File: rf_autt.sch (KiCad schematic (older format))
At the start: 10 parts, among them U4 FST3253

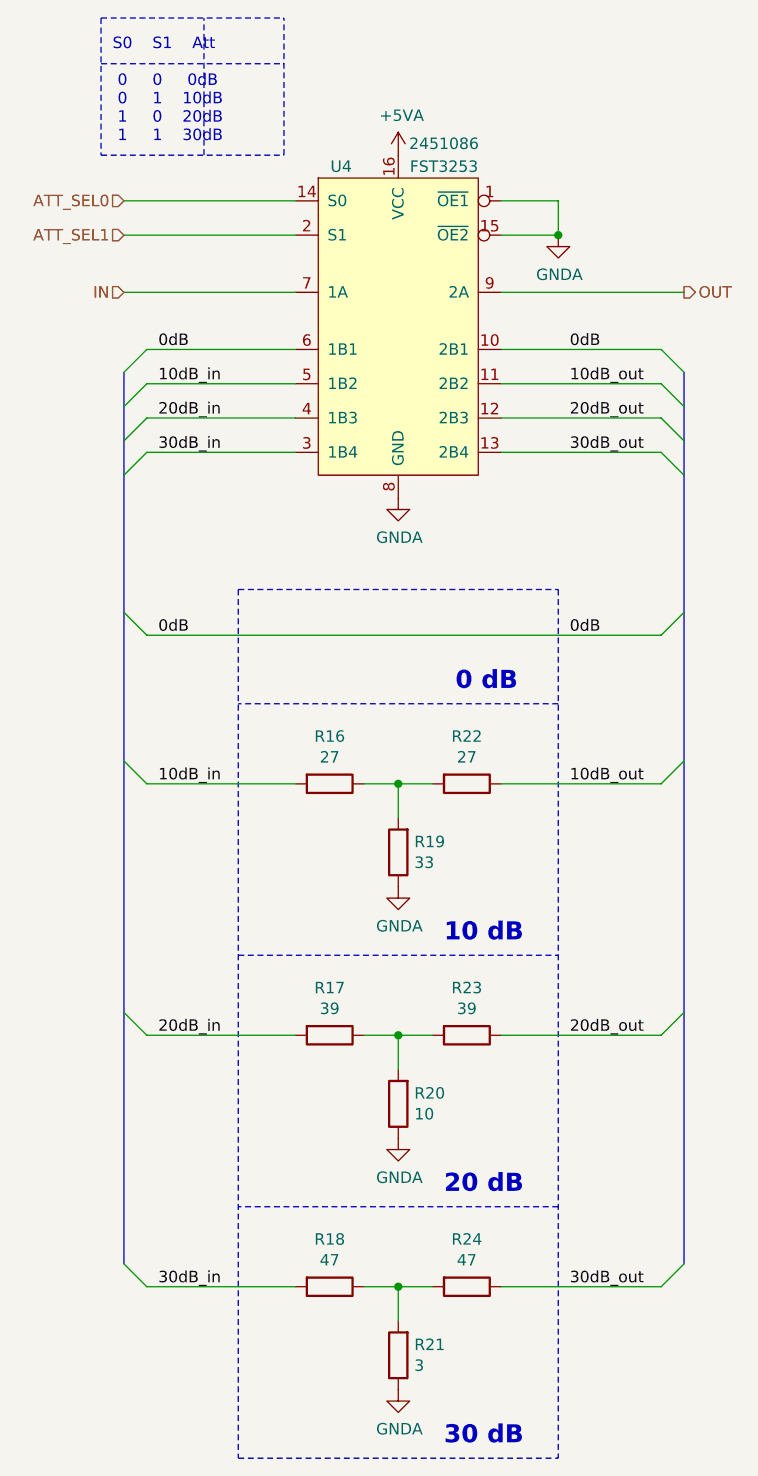
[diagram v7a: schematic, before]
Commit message: FPGA change and new project file
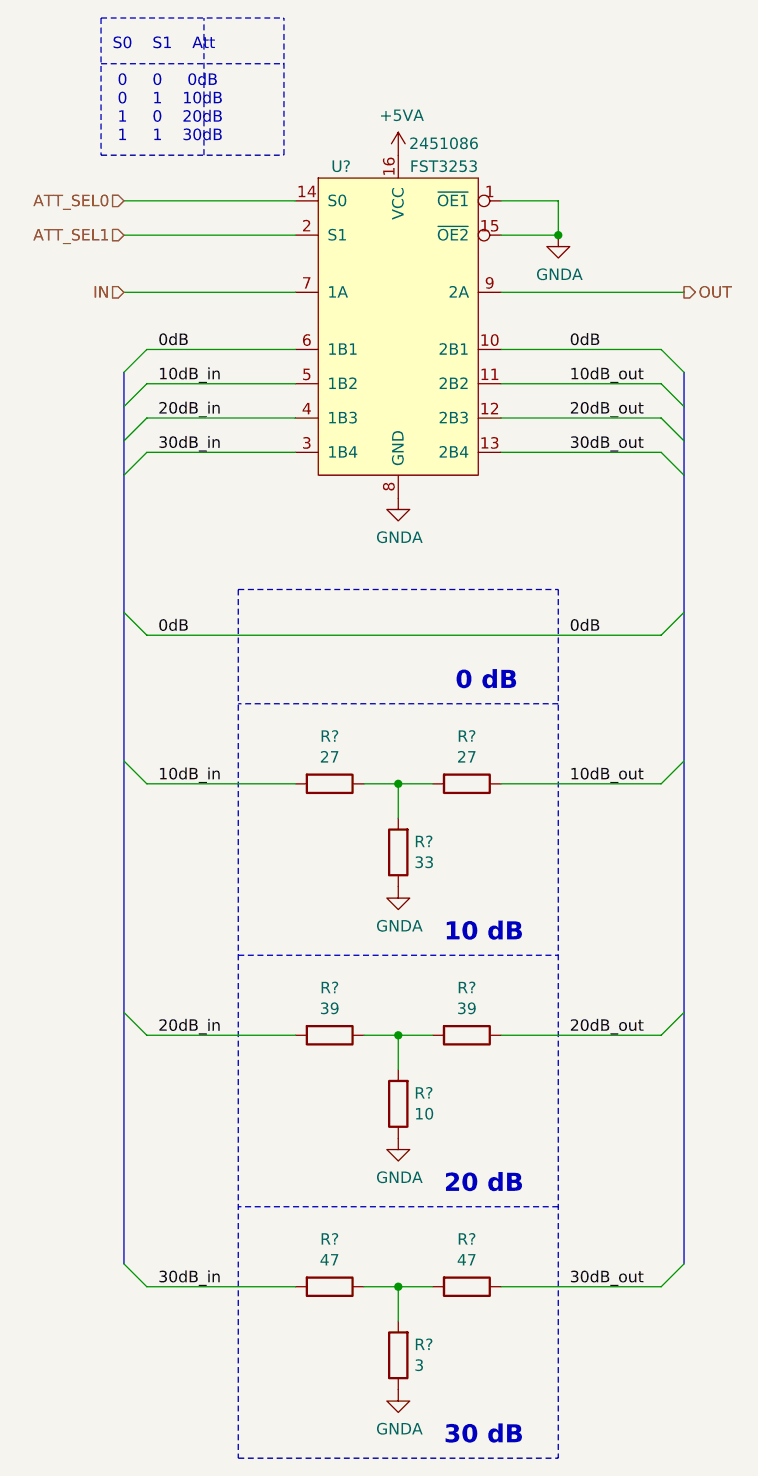
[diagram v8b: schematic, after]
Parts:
- renumbered R19 to R?, R16 to R?, R22 to R?, R21 to R?, R18 to R?, R24 to R?, R20 to R?, R17 to R?, R23 to R?, U4 to U?
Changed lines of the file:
@@
 $Descr A4 11693 8268
 encoding utf-8
-Sheet 7 7
+Sheet 7 12
 Title "HF-SDR RF-Attenuator"
 Date "2020 december"
@@
 OUT
 $Comp
-L sdr:FST3253 U4
+L sdr:FST3253 U?
 U 1 1 5FE50A6B
 P 5600 1900
-F 0 "U4" H 5350 2550 50  0000 C CNN
+F 0 "U?" H 5350 2550 50  0000 C CNN
 F 1 "FST3253" H 5800 2550 50  0000 C CNN
 F 2 "Package_SO:TSSOP-16_4.4x5mm_P0.65mm" H 5600 1900 50  0001 C CNN
@@
 ATT_SEL1
 $Comp
-L power:GNDA #PWR0136
+L power:GNDA #PWR?
 U 1 1 5FE53082
 P 5600 4400
-F 0 "#PWR0136" H 5600 4150 50  0001 C CNN
+F 0 "#PWR?" H 5600 4150 50  0001 C CNN
 F 1 "GNDA" H 5605 4227 50  0000 C CNN
 F 2 "" H 5600 4400 50  0001 C CNN
@@
 $EndComp
 $Comp
-L Device:R R19
+L Device:R R?
 U 1 1 5FE56E4E
 P 5600 4250
-F 0 "R19" H 5530 4204 50  0000 R CNN
+F 0 "R?" H 5530 4204 50  0000 R CNN
 F 1 "33" H 5530 4295 50  0000 R CNN
 F 2 "Resistor_SMD:R_0805_2012Metric_Pad1.20x1.40mm_HandSolder" V 5530 4250 50  0001 C CNN
@@
 $EndComp
 $Comp
-L Device:R R16
+L Device:R R?
 U 1 1 5FE5744A
 P 5300 3950
-F 0 "R16" V 5093 3950 50  0000 C CNN
+F 0 "R?" V 5093 3950 50  0000 C CNN
 F 1 "27" V 5184 3950 50  0000 C CNN
 F 2 "Resistor_SMD:R_0805_2012Metric_Pad1.20x1.40mm_HandSolder" V 5230 3950 50  0001 C CNN
@@
 $EndComp
 $Comp
-L Device:R R22
+L Device:R R?
 U 1 1 5FE57E99
 P 5900 3950
-F 0 "R22" V 5693 3950 50  0000 C CNN
+F 0 "R?" V 5693 3950 50  0000 C CNN
 F 1 "27" V 5784 3950 50  0000 C CNN
 F 2 "Resistor_SMD:R_0805_2012Metric_Pad1.20x1.40mm_HandSolder" V 5830 3950 50  0001 C CNN
@@
 	5600 3950 5750 3950
 $Comp
-L power:GNDA #PWR0137
+L power:GNDA #PWR?
 U 1 1 5FE5C53B
 P 5600 6600
-F 0 "#PWR0137" H 5600 6350 50  0001 C CNN
+F 0 "#PWR?" H 5600 6350 50  0001 C CNN
 F 1 "GNDA" H 5605 6427 50  0000 C CNN
 F 2 "" H 5600 6600 50  0001 C CNN
@@
 $EndComp
 $Comp
-L Device:R R21
+L Device:R R?
 U 1 1 5FE5C541
 P 5600 6450
-F 0 "R21" H 5530 6404 50  0000 R CNN
+F 0 "R?" H 5530 6404 50  0000 R CNN
 F 1 "3" H 5530 6495 50  0000 R CNN
 F 2 "Resistor_SMD:R_0805_2012Metric_Pad1.20x1.40mm_HandSolder" V 5530 6450 50  0001 C CNN
@@
 $EndComp
 $Comp
-L Device:R R18
+L Device:R R?
 U 1 1 5FE5C547
 P 5300 6150
-F 0 "R18" V 5093 6150 50  0000 C CNN
+F 0 "R?" V 5093 6150 50  0000 C CNN
 F 1 "47" V 5184 6150 50  0000 C CNN
 F 2 "Resistor_SMD:R_0805_2012Metric_Pad1.20x1.40mm_HandSolder" V 5230 6150 50  0001 C CNN
@@
 $EndComp
 $Comp
-L Device:R R24
+L Device:R R?
 U 1 1 5FE5C54D
 P 5900 6150
-F 0 "R24" V 5693 6150 50  0000 C CNN
+F 0 "R?" V 5693 6150 50  0000 C CNN
 F 1 "47" V 5784 6150 50  0000 C CNN
 F 2 "Resistor_SMD:R_0805_2012Metric_Pad1.20x1.40mm_HandSolder" V 5830 6150 50  0001 C CNN
@@
 	5600 6150 5750 6150
 $Comp
-L power:GNDA #PWR0138
+L power:GNDA #PWR?
 U 1 1 5FE5CA2D
 P 5600 5500
-F 0 "#PWR0138" H 5600 5250 50  0001 C CNN
+F 0 "#PWR?" H 5600 5250 50  0001 C CNN
 F 1 "GNDA" H 5605 5327 50  0000 C CNN
 F 2 "" H 5600 5500 50  0001 C CNN
@@
 $EndComp
 $Comp
-L Device:R R20
+L Device:R R?
 U 1 1 5FE5CA33
 P 5600 5350
-F 0 "R20" H 5530 5304 50  0000 R CNN
+F 0 "R?" H 5530 5304 50  0000 R CNN
 F 1 "10" H 5530 5395 50  0000 R CNN
 F 2 "Resistor_SMD:R_0805_2012Metric_Pad1.20x1.40mm_HandSolder" V 5530 5350 50  0001 C CNN
@@
 $EndComp
 $Comp
-L Device:R R17
+L Device:R R?
 U 1 1 5FE5CA39
 P 5300 5050
-F 0 "R17" V 5093 5050 50  0000 C CNN
+F 0 "R?" V 5093 5050 50  0000 C CNN
 F 1 "39" V 5184 5050 50  0000 C CNN
 F 2 "Resistor_SMD:R_0805_2012Metric_Pad1.20x1.40mm_HandSolder" V 5230 5050 50  0001 C CNN
@@
 $EndComp
 $Comp
-L Device:R R23
+L Device:R R?
 U 1 1 5FE5CA3F
 P 5900 5050
-F 0 "R23" V 5693 5050 50  0000 C CNN
+F 0 "R?" V 5693 5050 50  0000 C CNN
 F 1 "39" V 5784 5050 50  0000 C CNN
 F 2 "Resistor_SMD:R_0805_2012Metric_Pad1.20x1.40mm_HandSolder" V 5830 5050 50  0001 C CNN
@@
 	4300 800  5100 800
 $Comp
-L power:GNDA #PWR0139
+L power:GNDA #PWR?
 U 1 1 5FF9D7B5
 P 5600 2700
-F 0 "#PWR0139" H 5600 2450 50  0001 C CNN
+F 0 "#PWR?" H 5600 2450 50  0001 C CNN
 F 1 "GNDA" H 5605 2527 50  0000 C CNN
 F 2 "" H 5600 2700 50  0001 C CNN
@@
 $EndComp
 $Comp
-L power:GNDA #PWR0140
+L power:GNDA #PWR?
 U 1 1 5FF9DC72
 P 6300 1550
-F 0 "#PWR0140" H 6300 1300 50  0001 C CNN
+F 0 "#PWR?" H 6300 1300 50  0001 C CNN
 F 1 "GNDA" H 6305 1377 50  0000 C CNN
 F 2 "" H 6300 1550 50  0001 C CNN
@@
 Connection ~ 6300 1550
 $Comp
-L power:+5VA #PWR0141
+L power:+5VA #PWR?
 U 1 1 5FF9E701
 P 5600 1200
-F 0 "#PWR0141" H 5600 1050 50  0001 C CNN
+F 0 "#PWR?" H 5600 1050 50  0001 C CNN
 F 1 "+5VA" H 5615 1373 50  0000 C CNN
 F 2 "" H 5600 1200 50  0001 C CNN
